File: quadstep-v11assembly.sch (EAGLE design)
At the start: 115 parts, among them U1 A4983, U3 A4983, U4 A4983, U5 A4983, X1 MSTBA4, X2 MSTBA4, X3 MSTBA4, X4 MSTBA4

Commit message: Clean-up of the layout.
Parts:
- removed C10, C11, C18, C19, C21, C22, C23, C27, C28, C29, C3, C4, C46, C47, C49: 0.1uF, SparkFun:CAP0402-CAP
- removed C20, C6, C8: 0.22uF, SparkFun:CAP0402-CAP
- removed JP1, JP14, JP15, JP2, JP7, JP8: (no value), SparkFun:M023.5MM_LOCK
- removed LED1, LED3, LED4: green, SparkFun:LED0603
- removed R1, R18, R19, R2, R4, R5: 0.22, SparkFun:RESISTOR0805-RES
- removed R17, R24, R3: Trimpot, SparkFun:TRIMPOTSMD
- removed R20, R6, R66: 20k, SparkFun:RESISTOR0402-RES
- removed R21, R28, R7: 330, SparkFun:RESISTOR0402-RES
- removed R31, R32, R33, R37, R38, R39, R40, R45, R46, R47, R48, R8: 10k, SparkFun:RESISTOR0402-RES
- removed SJ14, SJ15, SJ16, SJ17, SJ2, SJ3, SJ4, SJ5, SJ6, SJ7, SJ8, SJ9: SOLDERJUMPERNO, SparkFun:SOLDERJUMPERNO
- removed TP1, TP2, TP3: TEST-POINT3X5, SparkFun:TEST-POINT3X5
- removed U1, U4, U5: A4983, SparkFun:A4983
- removed X1, X2, X4: MSTBA4, con-phoenix-508:MSTBA4
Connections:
- removed net DIR1: U1.DIR
- removed net DIR2: U5.DIR
- removed net DIR4: U4.DIR
- removed net MS11: R32.2, SJ4.2, U1.MS1
- removed net MS12: R38.2, SJ8.2, U5.MS1
- removed net MS14: R47.2, SJ16.2, U4.MS1
- removed net MS21: R31.2, SJ3.2, U1.MS2
- removed net MS22: R39.2, SJ7.2, U5.MS2
- removed net MS24: R46.2, SJ15.2, U4.MS2
- removed net MS31: R8.2, SJ2.2, U1.MS3
- removed net MS32: R40.2, SJ6.2, U5.MS3
- removed net MS34: R45.2, SJ14.2, U4.MS3
- removed net N$10: C47.1, U1.VCP
- removed net N$11: C8.1, U1.VREG
- removed net N$12: R66.1, U1.ROSC
- removed net N$13: C46.1, U1.CP1
- removed net N$14: R3.WIPER, TP1.1, U1.REF
- removed net N$15: C46.2, U1.CP2
- removed net N$17: LED1.C, R7.1
- removed net N$2: JP1.1, U1.OUT1B
- removed net N$3: JP1.2, U1.OUT1A
- removed net N$32: R18.2, U4.SENSE1
- removed net N$33: R19.2, U4.SENSE2
- removed net N$34: C19.1, U4.VCP
- removed net N$35: C20.1, U4.VREG
- removed net N$36: R20.1, U4.ROSC
- removed net N$37: R17.WIPER, TP3.1, U4.REF
- removed net N$38: C18.1, U4.CP1
- removed net N$39: C18.2, U4.CP2
- removed net N$40: LED3.C, R21.1
- removed net N$41: JP7.1, U4.OUT1B
- removed net N$42: JP7.2, U4.OUT1A
- removed net N$43: JP8.1, U4.OUT2A
- removed net N$44: JP8.2, U4.OUT2B
- removed net N$45: R1.2, U5.SENSE1
- removed net N$46: R2.2, U5.SENSE2
- removed net N$47: C4.1, U5.VCP
- removed net N$48: C6.1, U5.VREG
- removed net N$49: R6.1, U5.ROSC
- removed net N$50: R24.WIPER, TP2.1, U5.REF
- removed net N$51: C3.1, U5.CP1
- removed net N$52: C3.2, U5.CP2
- removed net N$53: LED4.C, R28.1
- removed net N$54: JP14.1, U5.OUT1B
- removed net N$55: JP14.2, U5.OUT1A
- removed net N$56: JP15.1, U5.OUT2A
- removed net N$57: JP15.2, U5.OUT2B
- removed net N$6: JP2.1, U1.OUT2A
- removed net N$7: JP2.2, U1.OUT2B
- removed net N$8: R4.2, U1.SENSE1
- removed net N$9: R5.2, U1.SENSE2
- removed net RST1: R33.2, SJ5.2, U1.RESET
- removed net RST2: R37.2, SJ9.2, U5.RESET
- removed net RST4: R48.2, SJ17.2, U4.RESET
- removed net STP1: LED1.A, U1.STEP
- removed net STP2: LED4.A, U5.STEP
- removed net STP4: LED3.A, U4.STEP
- net EN: no longer U1.ENABLE, U4.ENABLE, U5.ENABLE
- net GND: no longer C10.2, C11.2, C20.2, C21.2, C22.2, C23.2, C27.2, C28.2, C29.2, C49.2, C6.2, C8.2, R1.1, R17.CCW, R18.1, R19.1, R2.1, R20.2, R21.2, R24.CCW, R28.2, R3.CCW, R4.1, R5.1, R6.2, R66.2, R7.2, SJ14.1, SJ15.1, SJ16.1, SJ17.1, SJ2.1, SJ3.1, SJ4.1, SJ5.1, SJ6.1, SJ7.1, SJ8.1, SJ9.1, U1.GND@1, U1.GND@2, U1.GND_PAD, U4.GND@1, U4.GND@2, U4.GND_PAD, U5.GND@1, U5.GND@2, U5.GND_PAD
- net SLP: no longer U1.SLEEP, U4.SLEEP
- net VCC: no longer C10.1, C11.1, C19.2, C22.1, C23.1, C28.1, C29.1, C4.2, C47.2, U1.VBB1, U1.VBB2, U4.VBB1, U4.VBB2, U5.VBB1, U5.VBB2
- net VOUT: no longer C21.1, C27.1, C49.1, R17.CW, R24.CW, R3.CW, R31.1, R32.1, R33.1, R37.1, R38.1, R39.1, R40.1, R45.1, R46.1, R47.1, R48.1, R8.1, U1.VDD, U4.VDD, U5.VDD
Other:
- note removed: "CH1"
- note removed: "CH2"
- note removed: "CH4"

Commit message: Layout copied to the other three quadrants.
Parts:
- added C1, C10, C19, C2, C20, C22, C4, C7, C8: 0.1uF, SparkFun:CAP0603-CAP
- added C11, C18, C23, C24, C5, C6: 0.1uF, SparkFun:CAP0402-CAP
- added C21, C3, C9: 0.22uF, SparkFun:CAP0603-CAP
- added R1, R14, R24: Trimpot, SparkFun:TRIMPOTSMD
- added R12, R17, R18, R19, R20, R23, R26, R27, R28, R29, R3, R32, R4, R5, R6: 10k, SparkFun:RESISTOR0603-RES
- added R16, R2, R25: 20k, SparkFun:RESISTOR0603-RES
- added R21, R22, R30, R31, R7, R8: .11, SparkFun:RESISTOR2010
- added SJ14, SJ15, SJ16, SJ17, SJ2, SJ3, SJ4, SJ5, SJ6, SJ7, SJ8, SJ9: SOLDERJUMPERNO, SparkFun:SOLDERJUMPERNO
- added TP1, TP2, TP3: TEST-POINT3X5, SparkFun:TEST-POINT3X5
- added U1, U2, U4: A4983, SparkFun:A4983
- added X1, X2, X4: MSTBA4, con-phoenix-508:MSTBA4
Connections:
- net DIR3 renamed DIR-1
- net MS13 renamed MS1-1
- net MS23 renamed MS2-1
- net MS33 renamed MS3-1
- net RST3 renamed RST-1
- net STP3 renamed STP-1
- new net DIR-2: U2.DIR
- new net DIR-3: U1.DIR
- new net DIR-4: U4.DIR
- new net MS1-2: R19.2, SJ8.2, U2.MS1
- new net MS1-3: R5.2, SJ4.2, U1.MS1
- new net MS1-4: R28.2, SJ16.2, U4.MS1
- new net MS2-2: R18.2, SJ7.2, U2.MS2
- new net MS2-3: R4.2, SJ3.2, U1.MS2
- new net MS2-4: R27.2, SJ15.2, U4.MS2
- new net MS3-2: R17.2, SJ6.2, U2.MS3
- new net MS3-3: R3.2, SJ2.2, U1.MS3
- new net MS3-4: R26.2, SJ14.2, U4.MS3
- new net N$10: U1.OUT1A, X3-3.1
- new net N$11: U1.OUT2A, X3-2.1
- new net N$12: U1.OUT2B, X3-1.1
- new net N$13: U1.OUT1B, X3-4.1
- new net N$14: R7.2, U1.SENSE2
- new net N$15: R8.2, U1.SENSE1
- new net N$16: R1.CCW, R12.1
- new net N$17: C8.1, U2.VCP
- new net N$18: C9.1, U2.VREG
- new net N$2: C2.1, U1.VCP
- new net N$24: R16.1, U2.ROSC
- new net N$26: R14.WIPER, TP2.1, U2.REF
- new net N$3: C3.1, U1.VREG
- new net N$32: C7.1, U2.CP1
- new net N$33: C7.2, U2.CP2
- new net N$34: U2.OUT1A, X2-3.1
- new net N$35: U2.OUT2A, X2-2.1
- new net N$36: U2.OUT2B, X2-1.1
- new net N$37: U2.OUT1B, X2-4.1
- new net N$38: R21.2, U2.SENSE2
- new net N$39: R22.2, U2.SENSE1
- new net N$40: R14.CCW, R23.1
- new net N$41: C20.1, U4.VCP
- new net N$42: C21.1, U4.VREG
- new net N$43: R25.1, U4.ROSC
- new net N$44: R24.WIPER, TP3.1, U4.REF
- new net N$45: C19.1, U4.CP1
- new net N$46: C19.2, U4.CP2
- new net N$47: U4.OUT1A, X4-3.1
- new net N$48: U4.OUT2A, X4-2.1
- new net N$49: U4.OUT2B, X4-1.1
- new net N$50: U4.OUT1B, X4-4.1
- new net N$51: R30.2, U4.SENSE2
- new net N$52: R31.2, U4.SENSE1
- new net N$53: R24.CCW, R32.1
- new net N$6: R2.1, U1.ROSC
- new net N$7: R1.WIPER, TP1.1, U1.REF
- new net N$8: C1.1, U1.CP1
- new net N$9: C1.2, U1.CP2
- new net RST-2: R20.2, SJ9.2, U2.RESET
- new net RST-3: R6.2, SJ5.2, U1.RESET
- new net RST-4: R29.2, SJ17.2, U4.RESET
- new net STP-2: U2.STEP
- new net STP-3: U1.STEP
- new net STP-4: U4.STEP
- net EN: now also U1.ENABLE, U2.ENABLE, U4.ENABLE
- net GND: now also C10.2, C11.2, C18.2, C21.2, C22.2, C23.2, C24.2, C3.2, C4.2, C5.2, C6.2, C9.2, R1.CW, R14.CW, R16.2, R2.2, R21.1, R22.1, R24.CW, R25.2, R30.1, R31.1, R7.1, R8.1, SJ14.1, SJ15.1, SJ16.1, SJ17.1, SJ2.1, SJ3.1, SJ4.1, SJ5.1, SJ6.1, SJ7.1, SJ8.1, SJ9.1, U1.GND@1, U1.GND@2, U1.GND_PAD, U2.GND@1, U2.GND@2, U2.GND_PAD, U4.GND@1, U4.GND@2, U4.GND_PAD
- net N$28: now also X1-4.1; no longer X3-4.1
- net N$29: now also X1-3.1; no longer X3-3.1
- net N$30: now also X1-2.1; no longer X3-2.1
- net N$31: now also X1-1.1; no longer X3-1.1
- net SLP: now also U1.SLEEP, U2.SLEEP, U4.SLEEP
- net VCC: now also C11.1, C18.1, C2.2, C20.2, C23.1, C24.1, C5.1, C6.1, C8.2, U1.VBB1, U1.VBB2, U2.VBB1, U2.VBB2, U4.VBB1, U4.VBB2
- net VOUT: now also C10.1, C22.1, C4.1, R12.2, R17.1, R18.1, R19.1, R20.1, R23.2, R26.1, R27.1, R28.1, R29.1, R3.1, R32.2, R4.1, R5.1, R6.1, U1.VDD, U2.VDD, U4.VDD
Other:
- note added: "CH1"
- note added: "CH2"
- note added: "CH4"

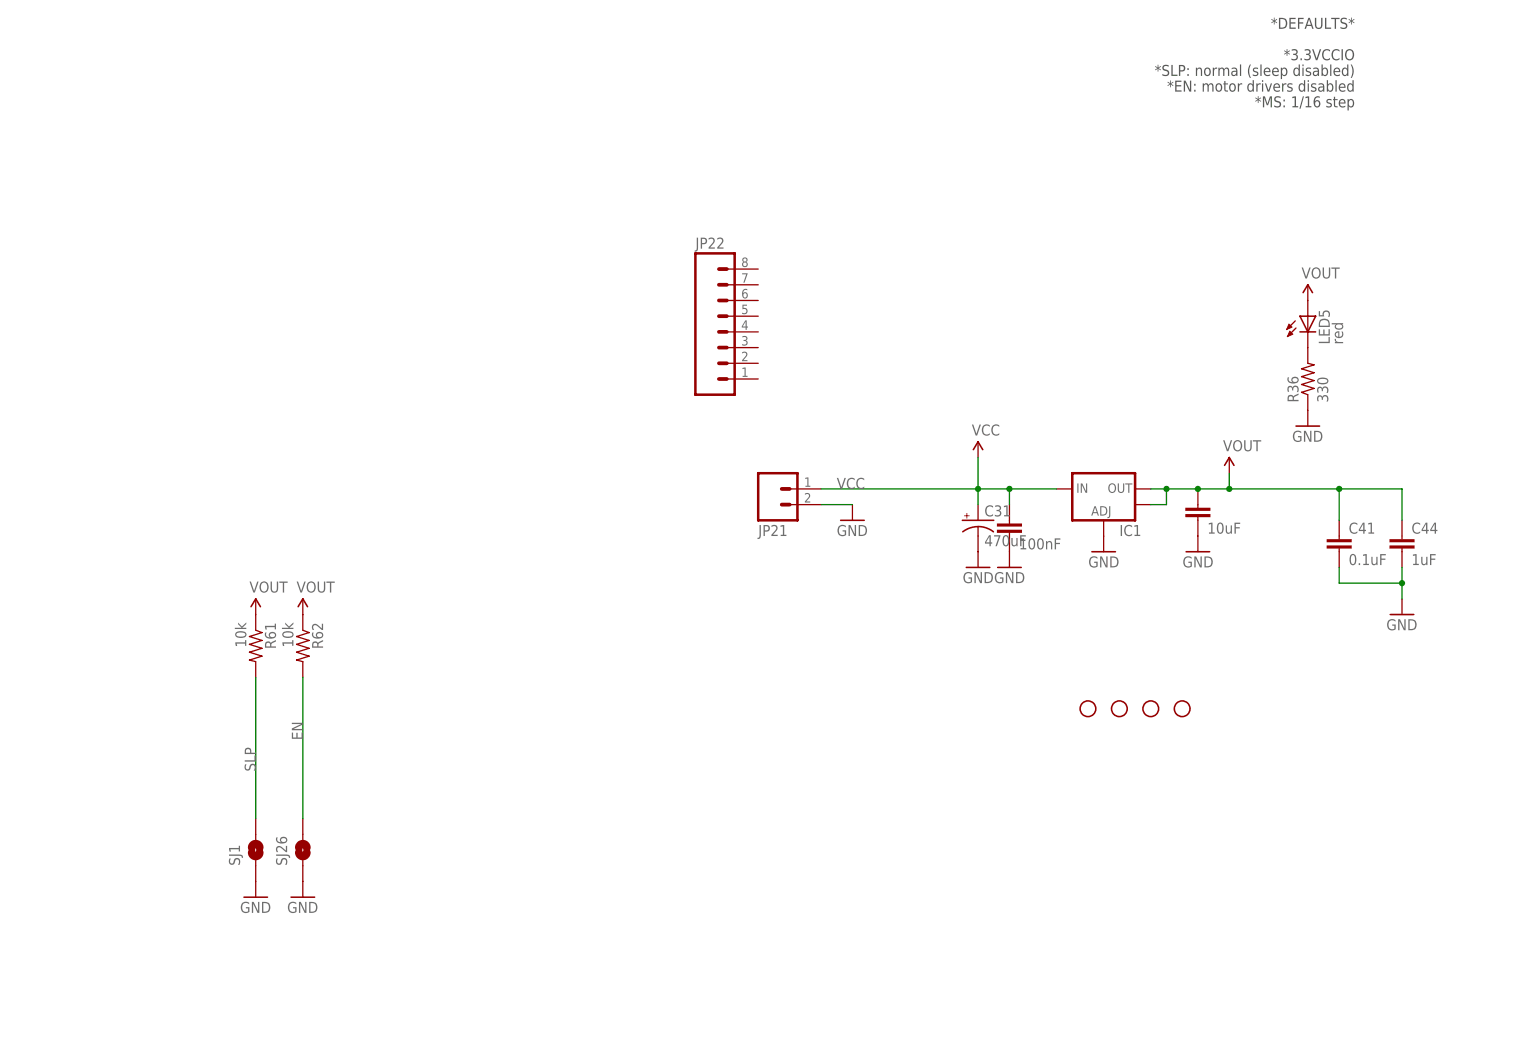
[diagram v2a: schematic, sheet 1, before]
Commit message: Adding a uC with USB
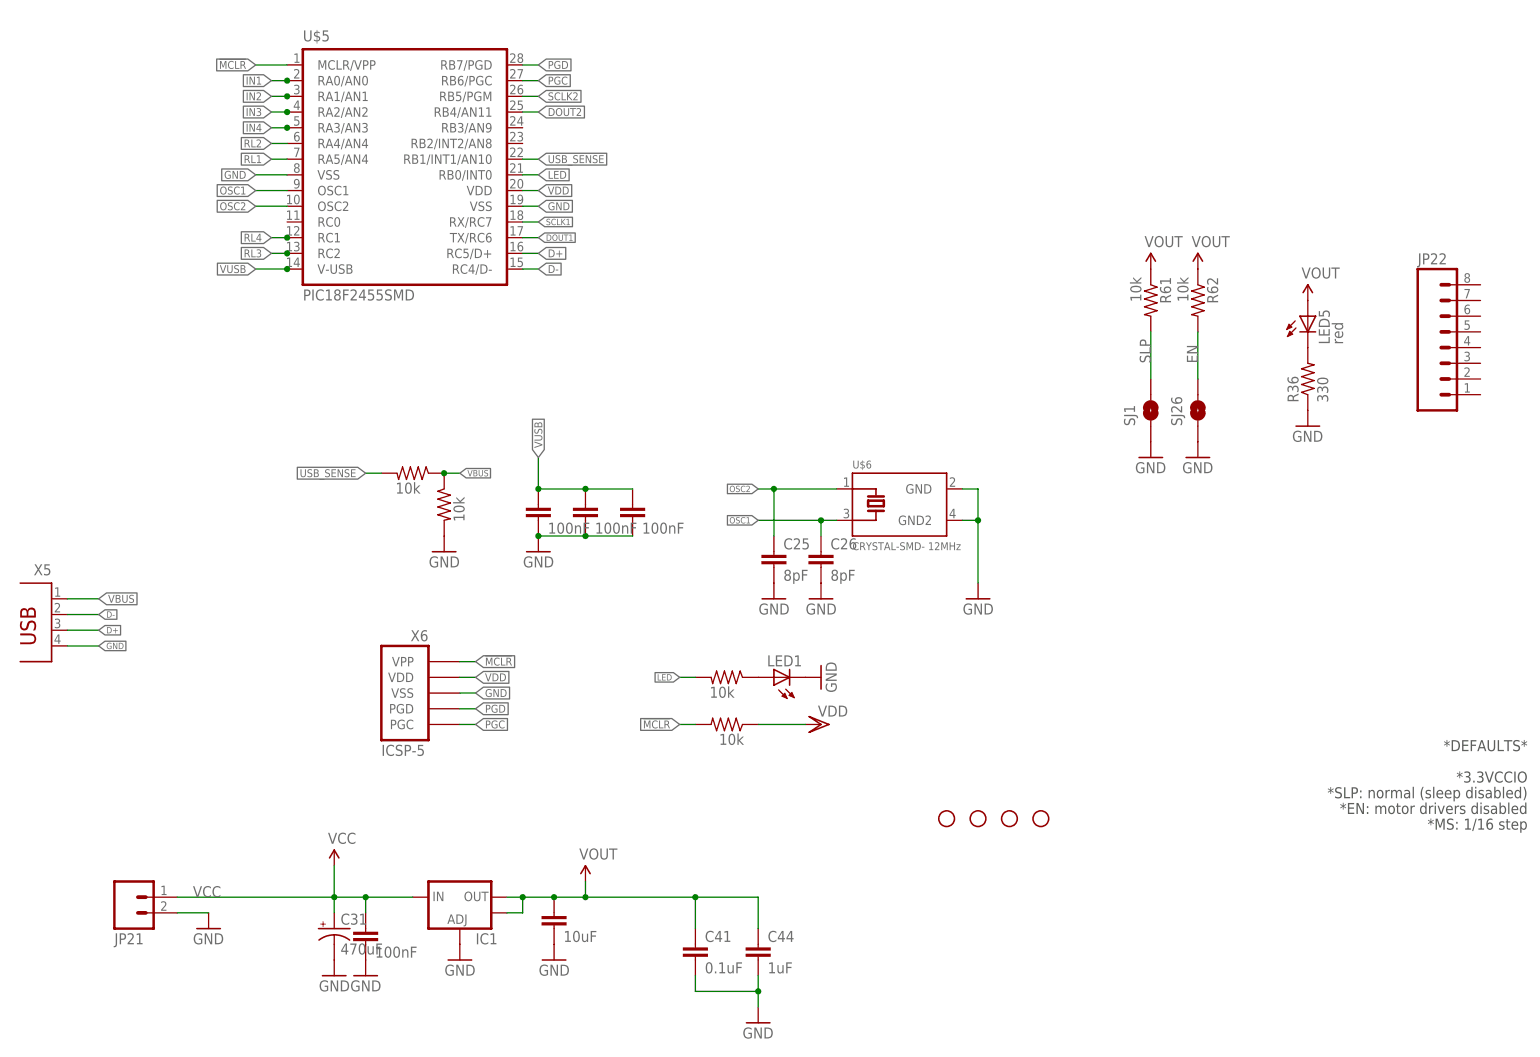
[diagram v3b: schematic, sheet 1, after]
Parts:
- added C25, C26: 8pF, SparkFun:CAP0603-CAP
- added C27, C28, C29: 100nF, SparkFun:CAP0805
- added LED1: (no value), led:LEDCHIPLED_0805
- added R33, R34, R35, R37: 10k, SparkFun:RESISTOR
- added U$5: PIC18F2455SMD, SparkFun:PIC18F2455SMD
- added U$6: CRYSTAL-SMD- 12MHz, crystal:CRYSTAL-SMD
- added X5: (no value), con-berg:PN61729
- added X6: ICSP-5, ICSP:ICSP-5
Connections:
- new net !MCLR: R34.2, U$5.MCLR/VPP, X6.VPP
- new net D+: U$5.RC5/D+, X5.3
- new net D-: U$5.RC4/D-, X5.2
- new net DOUT1: U$5.TX/RC6
- new net DOUT2: U$5.RB4/AN11
- new net IN1: U$5.RA0/AN0
- new net IN2: U$5.RA1/AN1
- new net IN3: U$5.RA2/AN2
- new net IN4: U$5.RA3/AN3
- new net LED: R33.2, U$5.RB0/INT0
- new net N$54: LED1.A, R33.1
- new net OSC1: C26.1, U$5.OSC1, U$6.OSC2
- new net OSC2: C25.1, U$5.OSC2, U$6.OSC1
- new net PGC: U$5.RB6/PGC, X6.PGC
- new net PGD: U$5.RB7/PGD, X6.PGD
- new net RL1: U$5.RA5/AN4
- new net RL2: U$5.RA4/AN4
- new net RL3: U$5.RC2
- new net RL4: U$5.RC1
- new net SCLK1: U$5.RX/RC7
- new net SCLK2: U$5.RB5/PGM
- new net USB_SENSE: R35.2, U$5.RB1/INT1/AN10
- new net VBUS: R35.1, R37.1, X5.1
- new net VDD: R34.1, U$5.VDD, X6.VDD
- new net VUSB: C27.2, C28.2, C29.2, U$5.V-USB
- net GND: now also C25.2, C26.2, C27.1, C28.1, C29.1, LED1.C, R37.2, U$5.VSS, U$5.VSS@19, U$6.GND, U$6.GND2, X5.4, X6.VSS
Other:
- moved on the sheet: C31, C41, C44, IC1, JP21, JP22, R61, R62, SJ1, SJ26

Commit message: Improving the layout
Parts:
- removed U$5: PIC18F2455SMD, SparkFun:PIC18F2455SMD
- added IC2: PIC18F2455_28W, microchip:PIC18F2455_28W
- C11, C16, C17, C18, C23, C24, C5, C6: device SparkFun:CAP0402-CAP -> SparkFun:CAP0603-CAP
- R61, R62: device SparkFun:RESISTOR0402-RES -> SparkFun:RESISTOR0603-RES
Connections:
- removed net IN1: U$5.RA0/AN0
- removed net IN2: U$5.RA1/AN1
- net !MCLR: now also IC2.!MCLR!/VPP/RE3; no longer U$5.MCLR/VPP
- net D+: now also IC2.RC5/D+/VP; no longer U$5.RC5/D+
- net D-: now also IC2.RC4/D-/VM; no longer U$5.RC4/D-
- net DIR-1: now also IC2.RA0/AN0
- net DIR-2: now also U1.DIR; no longer U2.DIR
- net DIR-3: now also U2.DIR; no longer U1.DIR
- net DOUT1: now also IC2.RC6/TX/CK; no longer U$5.TX/RC6
- net DOUT2: now also IC2.RB4/AN11/KBI0/CSSPP; no longer U$5.RB4/AN11
- net GND: now also IC2.VSS, IC2.VSS@1; no longer U$5.VSS, U$5.VSS@19
- net IN3: now also IC2.RA2/AN2/VREF-/CVREF; no longer U$5.RA2/AN2
- net IN4: now also IC2.RA3/AN3/VREF+; no longer U$5.RA3/AN3
- net LED: now also IC2.RB0/AN12/INT0/LFT0/SDI/SDA; no longer U$5.RB0/INT0
- net MS1-2: now also R5.2, SJ4.2, U1.MS1; no longer R19.2, SJ8.2, U2.MS1
- net MS1-3: now also R19.2, SJ8.2, U2.MS1; no longer R5.2, SJ4.2, U1.MS1
- net MS2-2: now also R4.2, SJ3.2, U1.MS2; no longer R18.2, SJ7.2, U2.MS2
- net MS2-3: now also R18.2, SJ7.2, U2.MS2; no longer R4.2, SJ3.2, U1.MS2
- net MS3-2: now also R3.2, SJ2.2, U1.MS3; no longer R17.2, SJ6.2, U2.MS3
- net MS3-3: now also R17.2, SJ6.2, U2.MS3; no longer R3.2, SJ2.2, U1.MS3
- net N$10: now also X2-3.1; no longer X3-3.1
- net N$11: now also X2-2.1; no longer X3-2.1
- net N$12: now also X2-1.1; no longer X3-1.1
- net N$13: now also X2-4.1; no longer X3-4.1
- net N$34: now also X3-3.1; no longer X2-3.1
- net N$35: now also X3-2.1; no longer X2-2.1
- net N$36: now also X3-1.1; no longer X2-1.1
- net N$37: now also X3-4.1; no longer X2-4.1
- net OSC1: now also IC2.OSC1/CLKI; no longer U$5.OSC1
- net OSC2: now also IC2.RA6/OSC2/CLKO; no longer U$5.OSC2
- net PGC: now also IC2.RB6/KBI2/PGC; no longer U$5.RB6/PGC
- net PGD: now also IC2.RB7/BKI3/PGD; no longer U$5.RB7/PGD
- net RL1: now also IC2.RA5/AN4/!SS!/HLVDIN/C2OUT; no longer U$5.RA5/AN4
- net RL2: now also IC2.RA4/T0CKI/CIOUT/RCV; no longer U$5.RA4/AN4
- net RL3: now also IC2.RC2/CCP1/P1A; no longer U$5.RC2
- net RL4: now also IC2.RC1/T1OSI/ICCP2/!UOE; no longer U$5.RC1
- net RST-2: now also R6.2, SJ5.2, U1.RESET; no longer R20.2, SJ9.2, U2.RESET
- net RST-3: now also R20.2, SJ9.2, U2.RESET; no longer R6.2, SJ5.2, U1.RESET
- net SCLK1: now also IC2.RC7/RX/DT/SDO; no longer U$5.RX/RC7
- net SCLK2: now also IC2.RB5/KBI1/PGM; no longer U$5.RB5/PGM
- net STP-1: now also IC2.RA1/AN1
- net STP-2: now also U1.STEP; no longer U2.STEP
- net STP-3: now also U2.STEP; no longer U1.STEP
- net USB_SENSE: now also IC2.RB1/AN10/INT1/SCK/SCL; no longer U$5.RB1/INT1/AN10
- net VDD: now also IC2.VDD; no longer U$5.VDD
- net VUSB: now also IC2.VUSB; no longer U$5.V-USB
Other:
- note removed: "CH2"
- note removed: "CH3"
- note removed: "CH4"
